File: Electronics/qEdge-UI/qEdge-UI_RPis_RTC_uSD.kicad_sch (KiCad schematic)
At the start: 66 parts, among them J301 RPi-4B_HAT, J302 1140084168, J303 Conn_01x20_Male, J304 Conn_01x20_Male, J305 Conn_01x20_Female, J306 Conn_01x20_Female, Q301 DMG2305UX, Q302 DMMT5401, Q303 DMG2305UX, SW301 KSC221J, U301 RPi-Pico, U302 PCF8523TS, Y301 32.768kHz

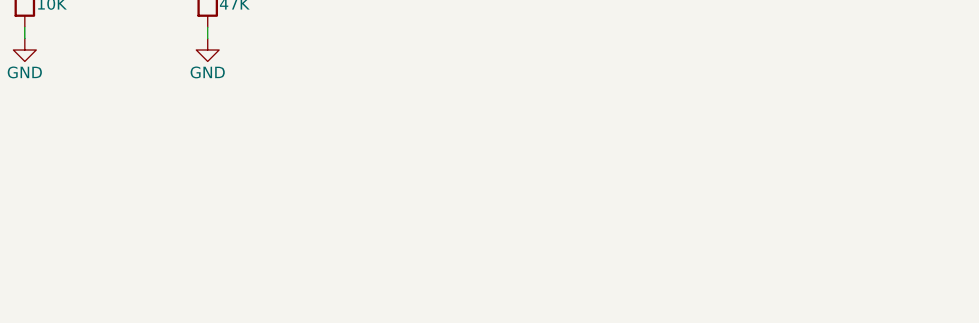
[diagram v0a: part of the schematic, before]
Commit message: added READMEs for Mechanic and Electronic added License in the Electronic schematics restructured Mechanics for better readability and reproducibility
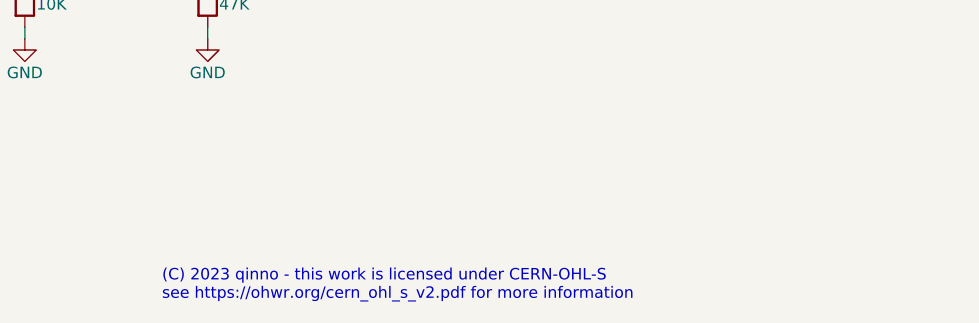
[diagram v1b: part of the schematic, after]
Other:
- note added: "(C) 2023 qinno - this work is licensed under CERN-OHL-S see https://ohwr.org/cern_ohl_s_v2.pdf for more information"
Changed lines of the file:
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@@
     (stroke (width 0) (type default) (color 0 0 0 0))
+  )
+  (text "(C) 2023 qinno - this work is licensed under CERN-OHL-S\nsee https://ohwr.org/cern_ohl_s_v2.pdf for more information"
+    (at 237.49 283.21 0)
+    (effects (font (size 1.27 1.27)) (justify left bottom))
   )
   (text "Pinheaders for RPi Pico" (at 321.31 36.83 0)
